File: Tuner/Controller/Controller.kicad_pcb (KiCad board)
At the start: 2 copper layers, 100 x 100 mm, 180 parts, among them J1 Conn_02x05_Odd_Even, J10 Conn_01x05, J11 Conn_Coaxial, J13 Conn_Coaxial, J15 Conn_01x02, J16 Conn_01x08, J18 Conn_01x01, J19 Conn_01x01, J2 Conn_02x05_Odd_Even, J20 Conn_01x01, J21 Conn_01x01, J3 Conn_02x05_Odd_Even, J4 Conn_02x05_Odd_Even, J5 Conn_02x05_Odd_Even, J6 Conn_01x02, J7 Conn_02x05_Odd_Even, J8 Conn_01x06, J9 Conn_Coaxial, Q1 2N3904, Q10 2N7000, Q11 2N7000, Q12 2N7000, Q2 2N3904, Q3 2N3904, Q4 2N3904, Q5 2N3904, Q6 2N3904, Q7 2N3904, Q8 2N3904, Q9 2N7000, U1 74LS393, U2 74HC14, U3 74HC86, U4 LM350_TO220

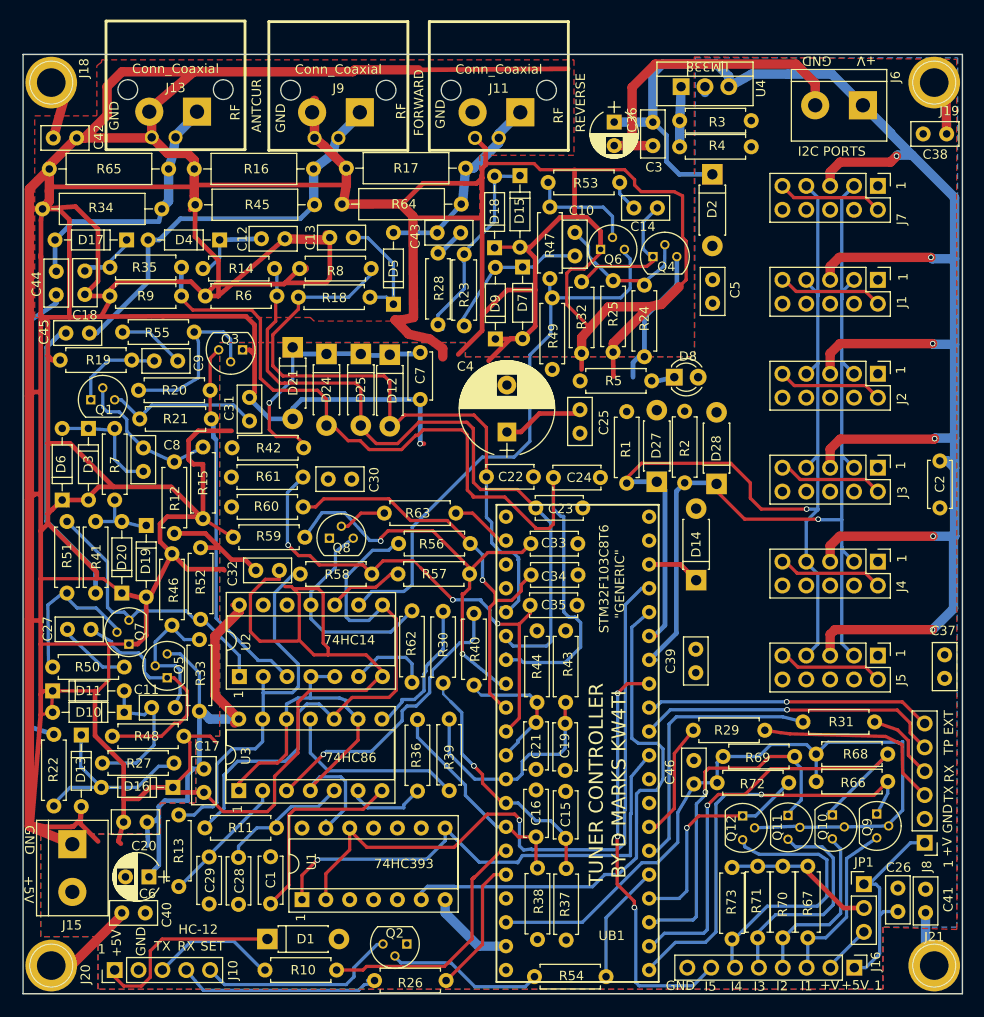
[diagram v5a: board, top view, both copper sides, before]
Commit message: Changed bypass method on delay lines
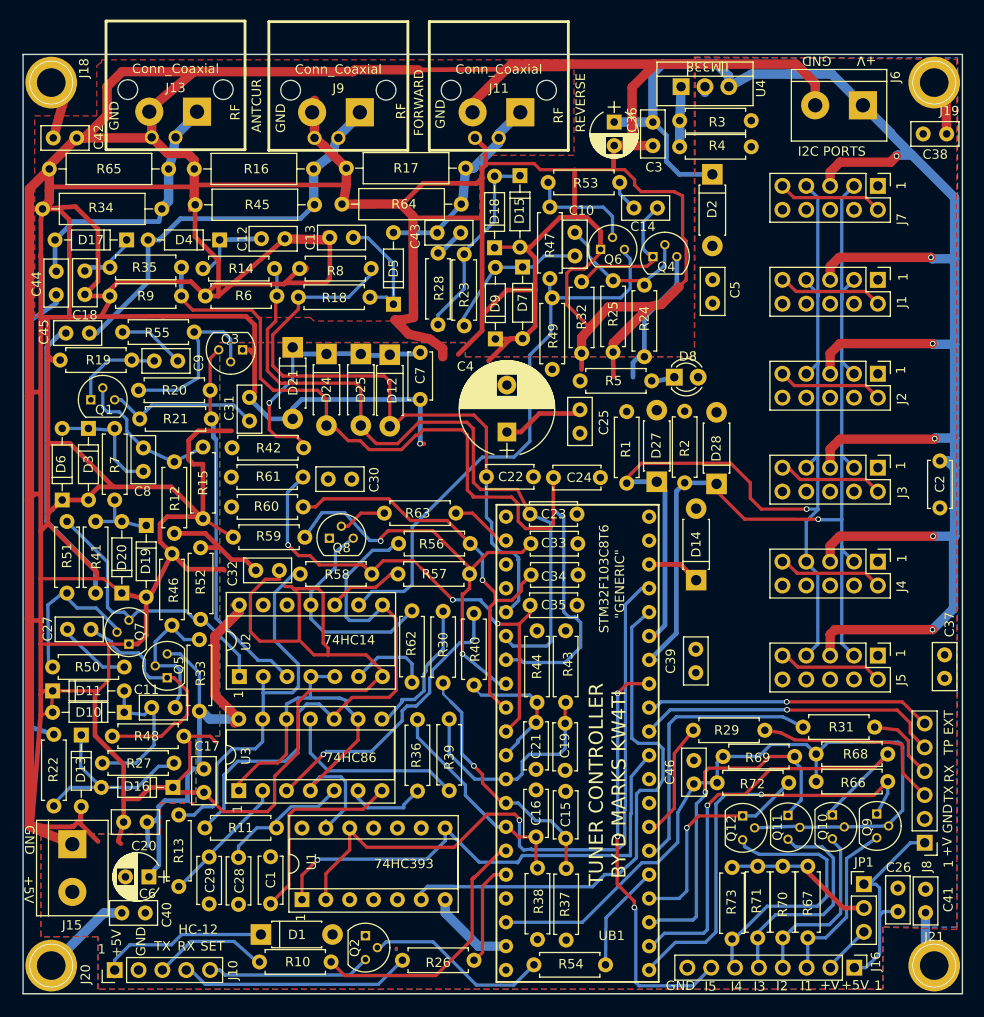
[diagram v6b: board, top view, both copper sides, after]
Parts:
- moved Q2 4.50 mm to (90.4, 121.8), turned to 270 degrees
- moved R26 3.67 mm to (102.0, 124.4)
- moved R54 1.26 mm to (116.0, 124.9)
- moved R10 1.04 mm to (86.8, 124.6)
- moved C23 0.90 mm to (108.0, 76.9)
- moved D1 0.84 mm to (79.3, 121.7)
- moved R31 0.55 mm to (144.7, 99.6)
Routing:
- net GND: track 956.7 -> 981.1 mm
- net Net-(J10-Pad5): track 21.6 -> 17.4 mm
- net Net-(R26-Pad1): track 14.7 -> 11.5 mm
- net Net-(D1-Pad1): track 21.6 -> 19.0 mm
- net Net-(Q2-Pad2): track 17.1 -> 19.7 mm
- net Net-(J10-Pad4): track 22.2 -> 24.7 mm
- net Net-(C40-Pad1): track 10.2 -> 12.2 mm
- net Net-(R10-Pad1): track 27.1 -> 28.6 mm
- net Net-(R54-Pad1): track 12.9 -> 11.6 mm
- net VCur: track 100.1 -> 101.2 mm
- net Net-(J10-Pad3): track 13.4 -> 12.4 mm

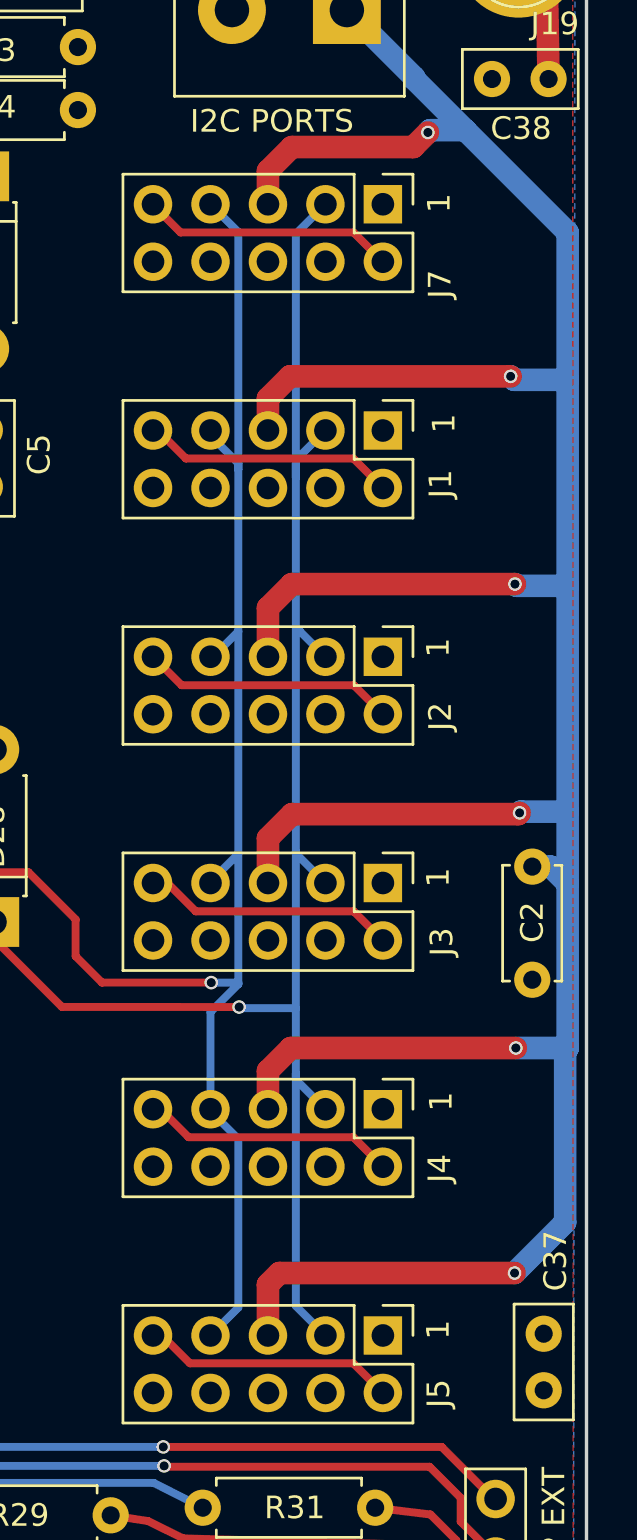
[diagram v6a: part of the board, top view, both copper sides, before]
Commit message: Changed I2C cable pinoutgit add Tunergit add Tuner Also added ICOM rig support
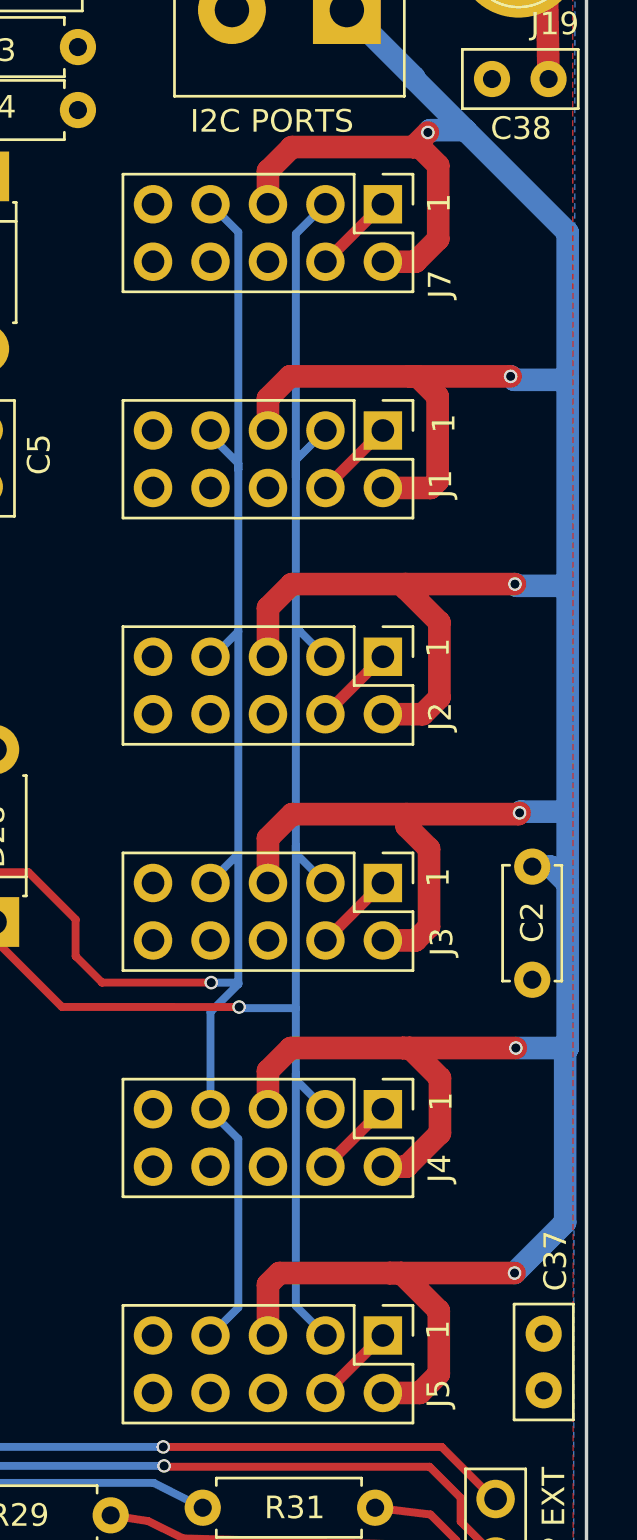
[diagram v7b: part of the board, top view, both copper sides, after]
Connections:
- J1 pad 2: +5V -> UPWR
- J2 pad 2: +5V -> UPWR
- J3 pad 2: +5V -> UPWR
- J4 pad 2: +5V -> UPWR
- J5 pad 2: +5V -> UPWR
- J7 pad 2: +5V -> UPWR
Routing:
- net +5V: track 199.9 -> 134.2 mm
- net UPWR: track 195.5 -> 243.3 mm
- net GND: track 981.1 -> 1002.7 mm

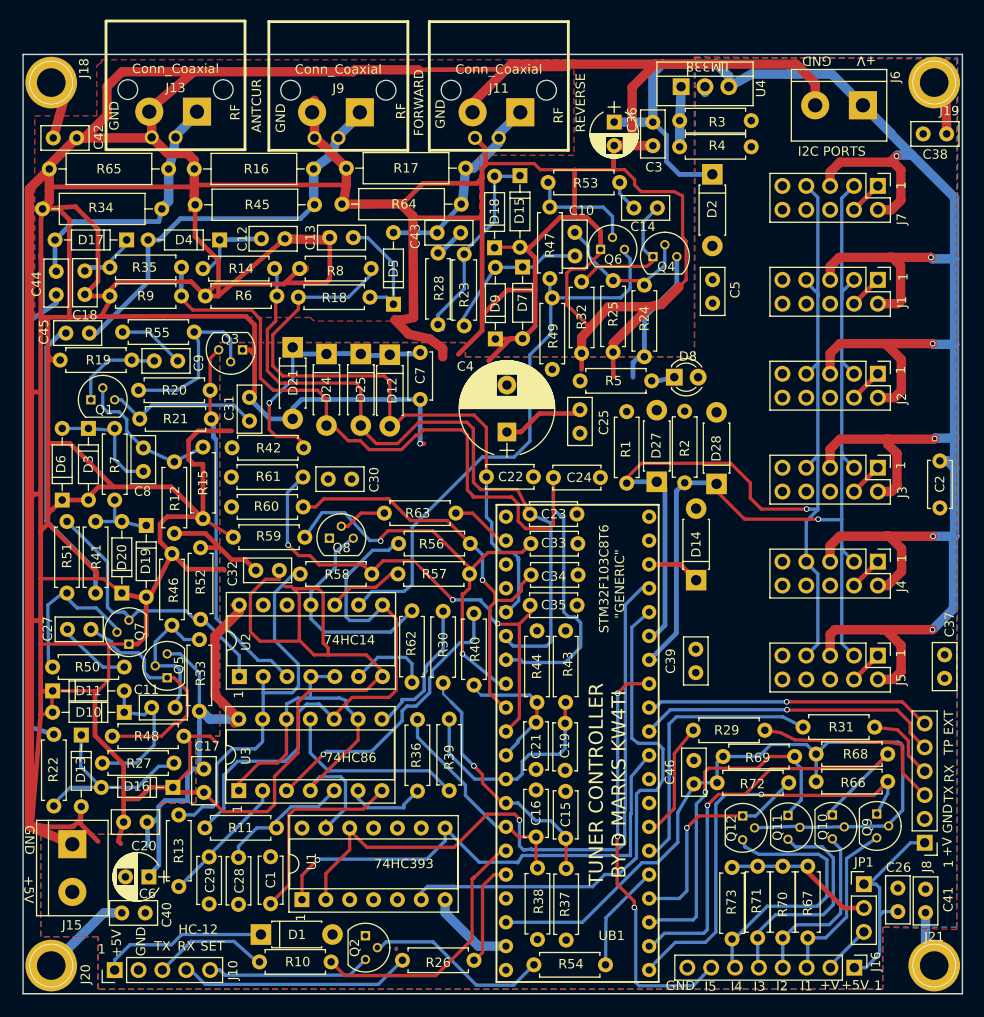
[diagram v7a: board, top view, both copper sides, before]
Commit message: Fixed icom tuning bad tuning report
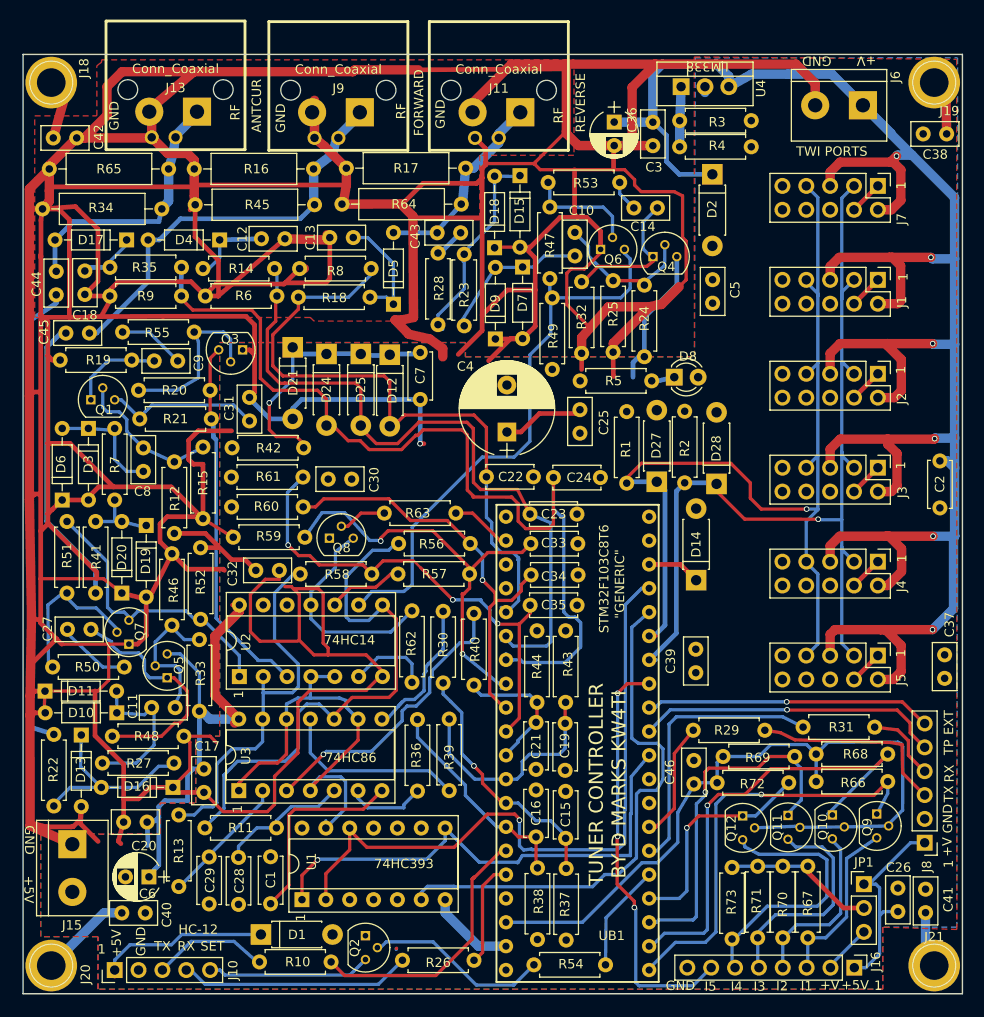
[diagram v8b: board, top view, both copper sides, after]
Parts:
- moved D11 0.81 mm to (56.3, 95.8)
- moved D10 0.79 mm to (64.0, 98.1)
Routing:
- net GND: track 1002.7 -> 1007.5 mm
- net Net-(C11-Pad1): track 15.9 -> 16.7 mm
- net FwdCurDlyDif: track 15.4 -> 14.7 mm
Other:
- board text added: "TWI PORTS"
- board text removed: "I2C PORTS"
